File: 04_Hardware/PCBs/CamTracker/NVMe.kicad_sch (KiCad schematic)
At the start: 57 parts, among them J28 Bus_M.2_Socket_M, U14 ASM2362, Y2 25MHz

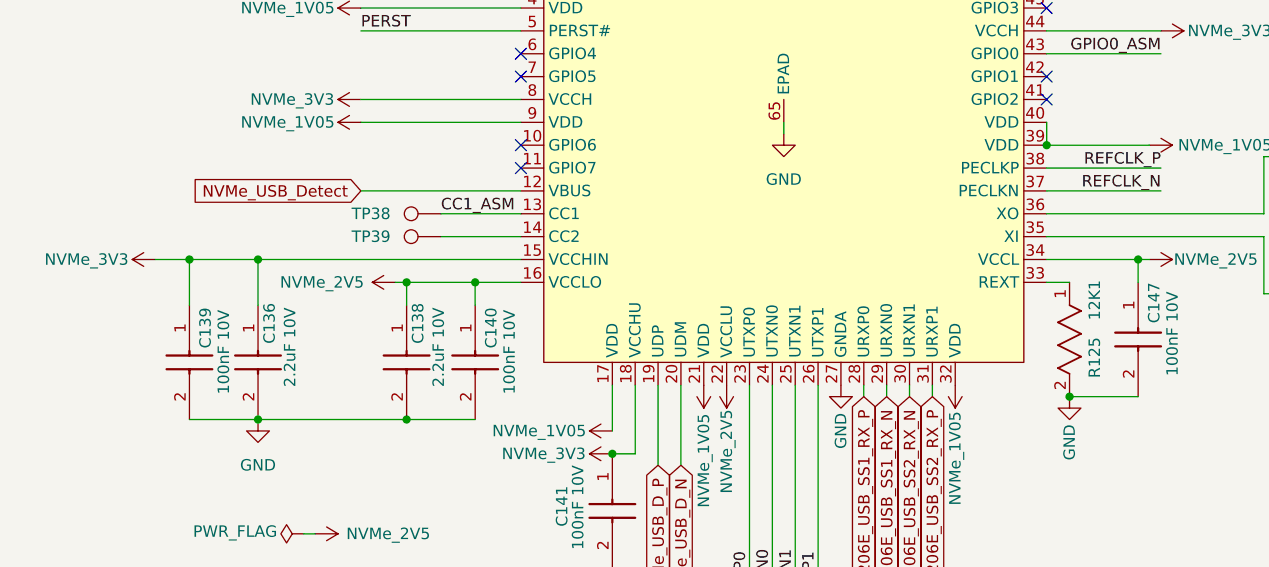
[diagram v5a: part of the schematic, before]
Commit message: feat(PCB): Updated NVME USB EN logic, turn-off the NVME 3V3 and 1V05 by EN pin
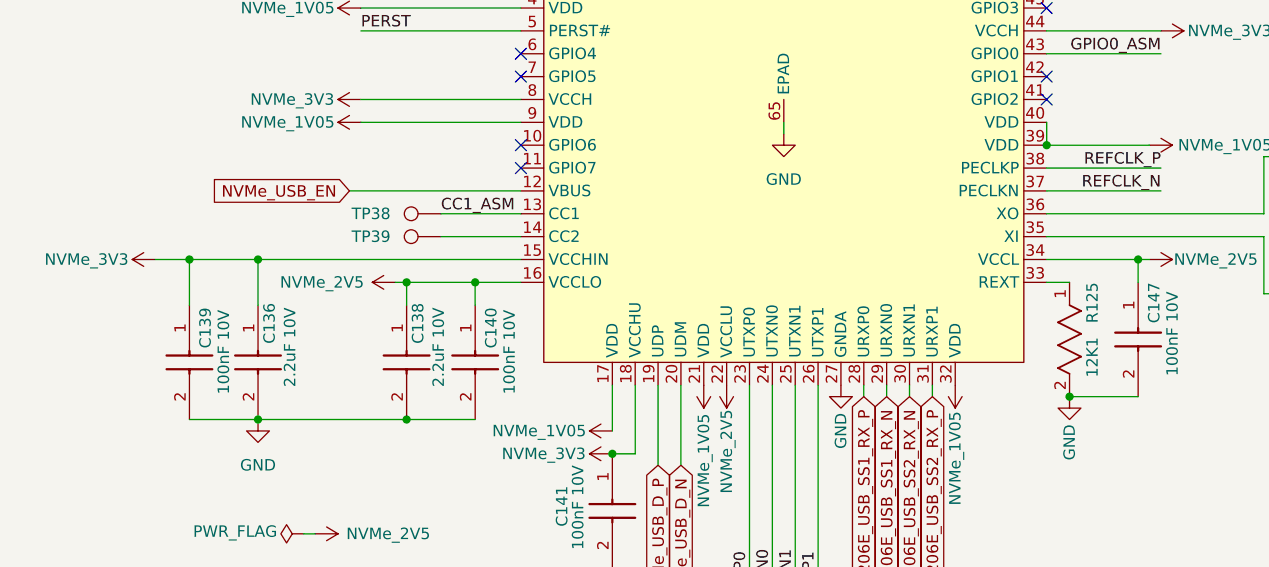
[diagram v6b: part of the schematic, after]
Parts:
- removed R125: 12K1, 000MCLib:RC0402N_YAG, symbol 000MCLib:RT1206FRE0712K1L
- added R125: 12K1, 000MCLib:RC0402N_YAG, symbol 000MCLib:RC0402FR-0712K1P
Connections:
- net GND: now also R125.2
- net at U14.33 (REXT): now also R125.1
- net NVMe_USB_Detect renamed NVMe_USB_EN
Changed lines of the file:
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@@
 	)
 	(junction
-		(at 165.1 148.59)
-		(diameter 0)
-		(color 0 0 0 0)
-	)
-	(junction
 		(at 139.7 30.48)
 		(diameter 0)
@@
 	)
 	(junction
+		(at 165.1 148.59)
+		(diameter 0)
+		(color 0 0 0 0)
+	)
+	(junction
 		(at 275.59 30.48)
 		(diameter 0)
@@
 	(wire
 		(pts
-			(xy 86.36 125.73) (xy 104.14 125.73)
+			(xy 85.09 125.73) (xy 104.14 125.73)
 		)
 		(stroke
@@
 		)
 	)
-	(global_label "NVMe_USB_Detect"
+	(global_label "SC206E_USB_SS1_TX_N"
 		(shape input)
-		(at 86.36 125.73 180)
+		(at 158.75 212.09 180)
 		(fields_autoplaced yes)
 		(effects
@@
 		)
 		(property "Intersheetrefs" "${INTERSHEET_REFS}"
-			(at 66.6833 125.73 0)
+			(at 133.6913 212.09 0)
 			(effects
 				(font
@@
 		)
 	)
-	(global_label "SC206E_USB_SS1_TX_N"
+	(global_label "NVMe_USB_D_N"
 		(shape input)
-		(at 158.75 212.09 180)
+		(at 121.92 156.21 270)
 		(fields_autoplaced yes)
 		(effects
@@
 		)
 		(property "Intersheetrefs" "${INTERSHEET_REFS}"
-			(at 133.6913 212.09 0)
+			(at 121.92 173.4676 90)
 			(effects
 				(font
@@
 		)
 	)
-	(global_label "NVMe_USB_D_N"
+	(global_label "SC206E_USB_SS1_RX_P"
 		(shape input)
-		(at 121.92 156.21 270)
+		(at 142.24 148.59 270)
 		(fields_autoplaced yes)
 		(effects
@@
 		)
 		(property "Intersheetrefs" "${INTERSHEET_REFS}"
-			(at 121.92 173.4676 90)
+			(at 142.24 173.8906 90)
 			(effects
 				(font
@@
 		)
 	)
-	(global_label "SC206E_USB_SS1_RX_P"
+	(global_label "SC206E_USB_SS2_RX_N"
 		(shape input)
-		(at 142.24 148.59 270)
+		(at 147.32 148.59 270)
 		(fields_autoplaced yes)
 		(effects
@@
 		)
 		(property "Intersheetrefs" "${INTERSHEET_REFS}"
-			(at 142.24 173.8906 90)
+			(at 147.32 173.9511 90)
 			(effects
 				(font
@@
 		)
 	)
-	(global_label "SC206E_USB_SS2_RX_N"
+	(global_label "SC206E_USB_SS1_RX_N"
 		(shape input)
-		(at 147.32 148.59 270)
+		(at 144.78 148.59 270)
 		(fields_autoplaced yes)
 		(effects
@@
 		)
 		(property "Intersheetrefs" "${INTERSHEET_REFS}"
-			(at 147.32 173.9511 90)
+			(at 144.78 173.9511 90)
 			(effects
 				(font
@@
 		)
 	)
-	(global_label "SC206E_USB_SS1_RX_N"
+	(global_label "NVMe_USB_EN"
 		(shape input)
-		(at 144.78 148.59 270)
+		(at 85.09 125.73 180)
 		(fields_autoplaced yes)
 		(effects
@@
 		)
 		(property "Intersheetrefs" "${INTERSHEET_REFS}"
-			(at 144.78 173.9511 90)
+			(at 68.921 125.73 0)
 			(effects
 				(font
@@
 	)
 	(symbol
-		(lib_id "000MCLib:RT1206FRE0712K1L")
-		(at 165.1 142.24 90)
-		(unit 1)
-		(exclude_from_sim no)
-		(in_bom yes)
-		(on_board yes)
-		(dnp no)
-		(property "Reference" "R125"
-			(at 167.894 141.986 0)
-			(effects
-				(font
-					(size 1.27 1.27)
-				)
-				(justify right)
-			)
-		)
-		(property "Value" "12K1"
-			(at 167.894 135.636 0)
-			(effects
-				(font
-					(size 1.27 1.27)
-				)
-				(justify right)
-			)
-		)
-		(property "Footprint" "000MCLib:RC0402N_YAG"
-			(at 165.1 148.59 0)
-			(effects
-				(font
-					(size 1.27 1.27)
-					(italic yes)
-				)
-				(hide yes)
-			)
-		)
-		(property "Datasheet" ""
-			(at 165.1 142.24 0)
-			(effects
-				(font
-					(size 1.27 1.27)
-					(italic yes)
-				)
-				(hide yes)
-			)
-		)
-		(property "Description" "Resistor 12K1 1/16W CH0402"
-			(at 165.1 148.59 0)
-			(effects
-				(font
-					(size 1.27 1.27)
-				)
-				(hide yes)
-			)
-		)
-		(property "Manufacturer" "YAGEO"
-			(at 165.1 142.24 0)
-			(effects
-				(font
-					(size 1.27 1.27)
-				)
-				(hide yes)
-			)
-		)
-		(property "Part Number" "RT1206FRE0712K1L"
-			(at 165.1 142.24 0)
-			(effects
-				(font
-					(size 1.27 1.27)
-				)
-				(hide yes)
-			)
-		)
-		(pin "1"
-		)
-		(pin "2"
-		)
-		(instances
-			(project ""
-				(path "/38605b01-fdd9-41de-8a8b-501279ee3e8a/50c8ebdc-55b9-4b13-889f-8a059ec3eb59"
-					(reference "R125")
-					(unit 1)
-				)
-			)
-		)
-	)
-	(symbol
 		(lib_id "power:GND")
 		(at 114.3 167.64 0)
@@
 					(unit 1)
 				)
+			)
+		)
+	)
+	(symbol
+		(lib_id "000MCLib:RC0402FR-0712K1P ")
+		(at 165.1 142.24 90)
+		(unit 1)
+		(exclude_from_sim no)
+		(in_bom yes)
+		(on_board yes)
+		(dnp no)
+		(property "Reference" "R125"
+			(at 167.64 135.89 0)
+			(effects
+				(font
+					(size 1.27 1.27)
+				)
+				(justify right)
+			)
+		)
+		(property "Value" "12K1"
+			(at 167.64 141.986 0)
+			(effects
+				(font
+					(size 1.27 1.27)
+				)
+				(justify right)
+			)
+		)
+		(property "Footprint" "000MCLib:RC0402N_YAG"
+			(at 165.1 148.59 0)
+			(effects
+				(font
+					(size 1.27 1.27)
+					(italic yes)
+				)
+				(hide yes)
+			)
+		)
+		(property "Datasheet" ""
+			(at 165.1 142.24 0)
+			(effects
+				(font
+					(size 1.27 1.27)
+					(italic yes)
+				)
+				(hide yes)
+			)
+		)
+		(property "Description" "Resistor 12K1 1/16W CH0402"
+			(at 165.1 148.59 0)
+			(effects
+				(font
+					(size 1.27 1.27)
+				)
+				(hide yes)
+			)
+		)
+		(property "Manufacturer" "YAGEO"
+			(at 165.1 142.24 0)
+			(effects
+				(font
+					(size 1.27 1.27)
+				)
+				(hide yes)
+			)
+		)
+		(property "Part Number" "RC0402FR-0712K1P "
+			(at 165.1 142.24 0)
+			(effects
+				(font
+					(size 1.27 1.27)
+				)
+				(hide yes)
+			)
+		)
+		(pin "2"
+		)
+		(pin "1"
+		)
+		(instances
+			(project "CamTracker"
+				(path "/38605b01-fdd9-41de-8a8b-501279ee3e8a/50c8ebdc-55b9-4b13-889f-8a059ec3eb59"
+					(reference "R125")
+					(unit 1)
+				)
